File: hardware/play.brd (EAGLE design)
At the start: 22.9 x 40 mm, 13 parts, among them T1 BC547, T2 BC547, T3 BC547, T4 BC547

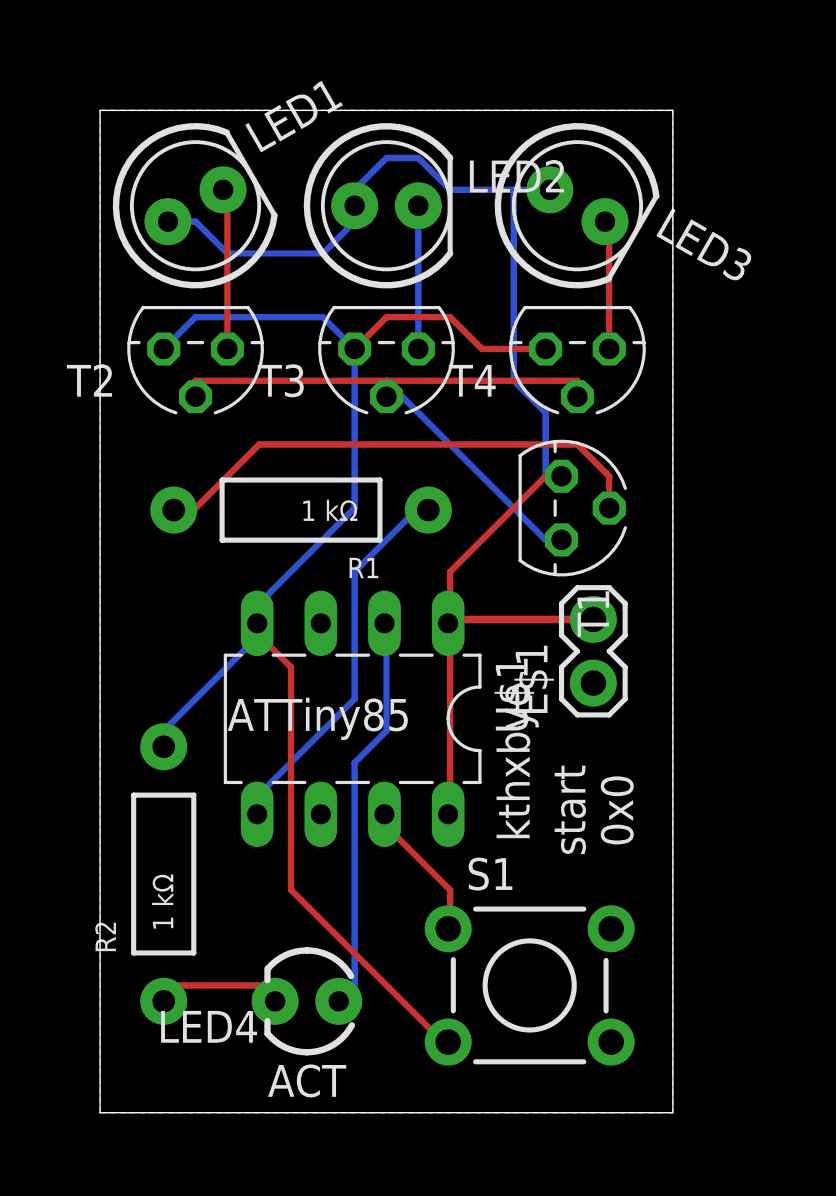
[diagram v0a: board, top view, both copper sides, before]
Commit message: Updated board to add the capacitor + play logo
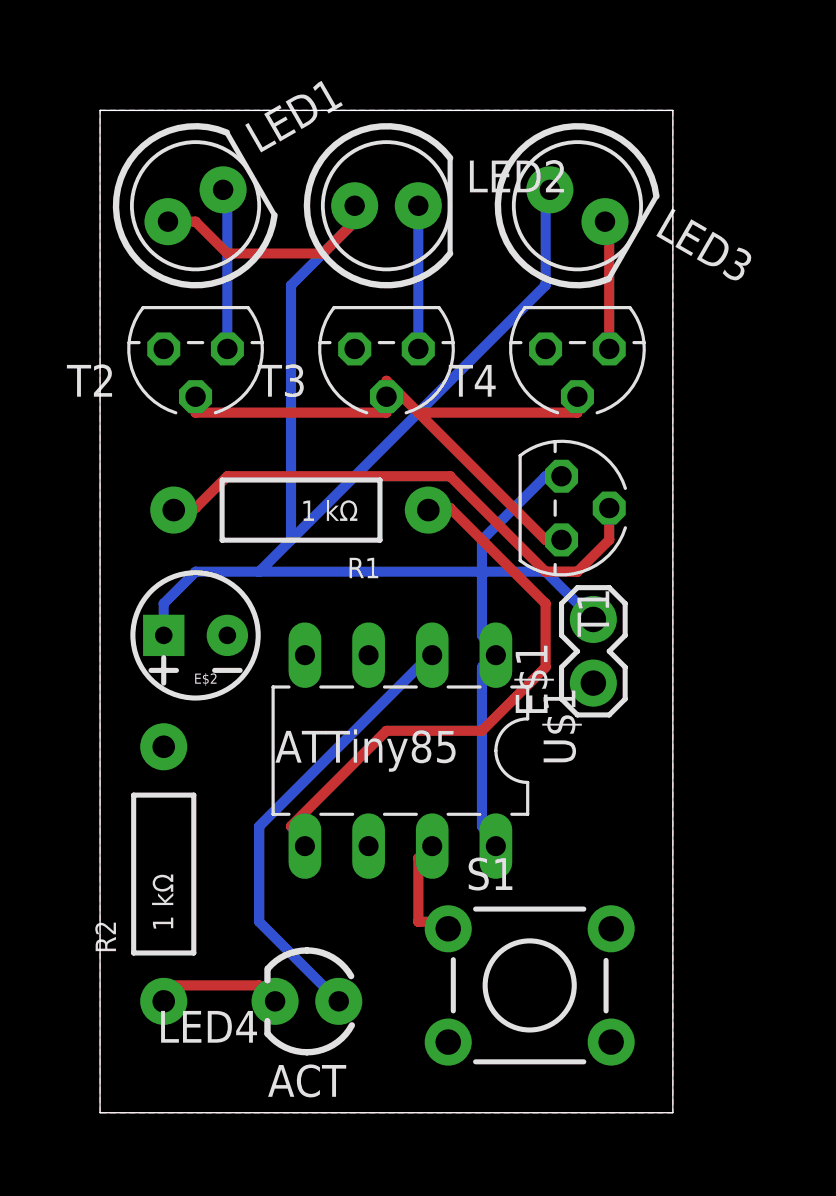
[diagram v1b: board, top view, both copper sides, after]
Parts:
- added E$2: (no value), SparkFun-Capacitors:CPOL-RADIAL-10UF-25V-KIT
- moved U$1 2.29 mm to (12.0, 14.4)
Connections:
- net GND: now also E$2.2
- net VCC: now also E$2.1
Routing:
- net GND: track 56.8 -> 0.00 mm
- net VCC: track 52.8 -> 80.6 mm
- net N$1: track 15.3 -> 22.6 mm
- net N$8: track 15.9 -> 18.0 mm
- net N$3: track 27.4 -> 26.1 mm
- net N$2: track 20.2 -> 21.3 mm
- net N$5: track 5.64 -> 4.83 mm
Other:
- board text added: "(play)"
- board text added: "0x00"
- board text removed: "kthxbye"
- board text removed: "start 0x0"

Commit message: New hardware PCB design, with signal connector
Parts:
- removed E$1: (no value), SparkFun-Connectors:1X02
- removed E$2: (no value), SparkFun-Capacitors:CPOL-RADIAL-10UF-25V-KIT
- added C1: 10µF, SparkFun-Capacitors:CPOL-RADIAL-10UF-25V
- added JP1, JP2: M02PTH, SparkFun-Connectors:1X02
- moved LED4 10.8 mm to (19.1, 3.81)
- moved R2 8.28 mm to (3.17, 17.8)
- moved R1 7.22 mm to (15.2, 24.1), turned to 0 degrees
- moved T1 5.75 mm to (19.1, 18.4)
- moved S1 5.71 mm to (11.4, 5.08), turned to 270 degrees
- moved U$1 2.16 mm to (10.9, 16.4), turned to 0 degrees
- moved T4 1.42 mm to (18.4, 29.2)
- moved T2 1.27 mm to (3.81, 29.2)
- moved T3 1.27 mm to (11.4, 29.2)
- moved LED3 0.96 mm to (18.6, 35.3)
- moved LED1 0.73 mm to (3.96, 35.5)
- moved LED2 0.63 mm to (11.4, 35.6)
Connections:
- net GND: now also C1.2, JP1.2, JP2.2; no longer E$1.1, E$2.2
- net N$2: now also JP2.1
- net VCC: now also C1.1, JP1.1; no longer E$1.2, E$2.1
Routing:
- net N$9: track 5.34 -> 19.0 mm
- net VCC: track 80.6 -> 68.4 mm
- net N$2: track 21.3 -> 12.1 mm
- net N$1: track 22.6 -> 14.6 mm
- net N$5: track 4.83 -> 11.0 mm
- net N$8: track 18.0 -> 20.0 mm
- net N$3: track 26.1 -> 27.3 mm
- net N$6: track 5.71 -> 6.35 mm
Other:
- board size 22.9 x 40 mm -> 22.5 x 40 mm
- board text added: "(this is not a bomb)"
- board text added: "PWR"
- board text added: "SGNL"
- board text added: "batch"
- board text removed: "ATTiny85"

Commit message: Updated hardware
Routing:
- net GND: track 0.00 -> 67.0 mm
- net VCC: track 68.4 -> 61.9 mm
- removed copper zone on layer 1, net GND
- removed copper zone on layer 16, net GND
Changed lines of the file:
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@@
 <signals>
 <signal name="VCC">
-<contactref element="U$1" pad="8"/>
+<contactref element="JP1" pad="1"/>
 <contactref element="U$1" pad="1"/>
 <contactref element="T1" pad="3"/>
@@
 <contactref element="LED3" pad="A"/>
 <contactref element="C1" pad="1"/>
-<contactref element="JP1" pad="1"/>
+<contactref element="U$1" pad="8"/>
 <wire x1="4.445" y1="33.02" x2="3.175" y2="34.29" width="0.4064" layer="16"/>
 <wire x1="6.35" y1="33.02" x2="4.445" y2="33.02" width="0.4064" layer="16"/>
@@
 <wire x1="10.16" y1="35.56" x2="10.16" y2="36.83" width="0.4064" layer="1"/>
 <wire x1="17.145" y1="36.195" x2="17.547571875" y2="35.962571875" width="0.4064" layer="1"/>
-<wire x1="5.08" y1="2.54" x2="5.08" y2="7.62" width="0.4064" layer="1"/>
 <wire x1="14.605" y1="20.32" x2="10.16" y2="20.32" width="0.4064" layer="1"/>
 <wire x1="10.16" y1="20.32" x2="7.62" y2="20.32" width="0.4064" layer="1"/>
 <wire x1="7.62" y1="20.32" x2="7.14" y2="20.16" width="0.4064" layer="1"/>
-<wire x1="14.605" y1="20.32" x2="14.76" y2="20.16" width="0.4064" layer="1"/>
 <wire x1="15.24" y1="19.685" x2="19.05" y2="19.685" width="0.4064" layer="1"/>
-<wire x1="15.24" y1="19.685" x2="14.76" y2="20.16" width="0.4064" layer="1"/>
 <wire x1="10.16" y1="12.7" x2="5.08" y2="7.62" width="0.4064" layer="1"/>
 <wire x1="10.16" y1="20.32" x2="10.16" y2="12.7" width="0.4064" layer="1"/>
 <wire x1="15.24" y1="33.655" x2="17.547571875" y2="35.962571875" width="0.4064" layer="1"/>
 <wire x1="15.24" y1="20.32" x2="15.24" y2="33.655" width="0.4064" layer="1"/>
-<wire x1="15.24" y1="20.32" x2="14.76" y2="20.16" width="0.4064" layer="1"/>
+<wire x1="14.76" y1="20.16" x2="15.24" y2="20.32" width="0" layer="19" extent="1-1"/>
+<wire x1="14.605" y1="20.32" x2="14.76" y2="20.16" width="0" layer="19" extent="1-1"/>
+<wire x1="15.24" y1="19.685" x2="15.24" y2="20.32" width="0" layer="19" extent="1-1"/>
+<wire x1="5.08" y1="2.54" x2="5.08" y2="7.62" width="0" layer="19" extent="1-1"/>
 </signal>
 <signal name="GND">
@@
 <contactref element="JP2" pad="2"/>
 <contactref element="JP1" pad="2"/>
-<polygon width="0.4064" layer="1" isolate="0.4064" thermals="no">
-<vertex x="0" y="40.005"/>
-<vertex x="22.5425" y="40.005"/>
-<vertex x="22.5425" y="0"/>
-<vertex x="0" y="0"/>
-</polygon>
-<polygon width="0.4064" layer="16" isolate="0.4064" thermals="no">
-<vertex x="0" y="40.005"/>
-<vertex x="22.5425" y="40.005"/>
-<vertex x="22.5425" y="0"/>
-<vertex x="0" y="0"/>
-</polygon>
-<polygon width="0.4064" layer="16" isolate="0.4064" thermals="no">
-<vertex x="0" y="40.005"/>
-<vertex x="22.5425" y="40.005"/>
-<vertex x="22.5425" y="0"/>
-<vertex x="0" y="0"/>
-</polygon>
+<wire x1="2.54" y1="23.495" x2="2.54" y2="29.21" width="0.4064" layer="1"/>
+<wire x1="3.175" y1="22.86" x2="2.54" y2="23.495" width="0.4064" layer="1"/>
+<wire x1="3.81" y1="22.86" x2="10.16" y2="29.21" width="0.4064" layer="16"/>
+<wire x1="3.175" y1="22.86" x2="3.81" y2="22.86" width="0.4064" layer="16"/>
+<wire x1="14.605" y1="29.21" x2="17.145" y2="29.21" width="0.4064" layer="16"/>
+<wire x1="13.335" y1="30.48" x2="14.605" y2="29.21" width="0.4064" layer="16"/>
+<wire x1="11.43" y1="30.48" x2="13.335" y2="30.48" width="0.4064" layer="16"/>
+<wire x1="10.16" y1="29.21" x2="11.43" y2="30.48" width="0.4064" layer="16"/>
+<wire x1="2.54" y1="7.62" x2="6.985" y2="12.065" width="0.4064" layer="1"/>
+<wire x1="6.985" y1="12.065" x2="7.14" y2="12.54" width="0.4064" layer="1"/>
+<wire x1="2.54" y1="7.62" x2="2.54" y2="2.54" width="0.4064" layer="1"/>
+<wire x1="3.81" y1="8.89" x2="8.89" y2="8.89" width="0.4064" layer="16"/>
+<wire x1="2.54" y1="7.62" x2="3.81" y2="8.89" width="0.4064" layer="16"/>
+<wire x1="8.89" y1="8.89" x2="9.1694" y2="8.3312" width="0.4064" layer="16"/>
+<wire x1="14.605" y1="6.985" x2="18.415" y2="10.795" width="0.4064" layer="1"/>
+<wire x1="10.795" y1="6.985" x2="14.605" y2="6.985" width="0.4064" layer="1"/>
+<wire x1="9.525" y1="8.255" x2="10.795" y2="6.985" width="0.4064" layer="1"/>
+<wire x1="9.525" y1="8.255" x2="9.1694" y2="8.3312" width="0.4064" layer="1"/>
+<wire x1="3.175" y1="16.51" x2="3.175" y2="22.86" width="0.4064" layer="1"/>
+<wire x1="6.985" y1="12.7" x2="3.175" y2="16.51" width="0.4064" layer="1"/>
+<wire x1="6.985" y1="12.7" x2="7.14" y2="12.54" width="0.4064" layer="1"/>
 </signal>
 <signal name="N$1">
